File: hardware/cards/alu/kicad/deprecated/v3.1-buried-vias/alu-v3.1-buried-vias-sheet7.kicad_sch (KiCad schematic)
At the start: 8 parts, among them IC1 74*04, IC27 74*86, IC33 74*86, IC34 74*86, IC35 74*283, IC36 74*283, IC37 74*244, IC6 74*08

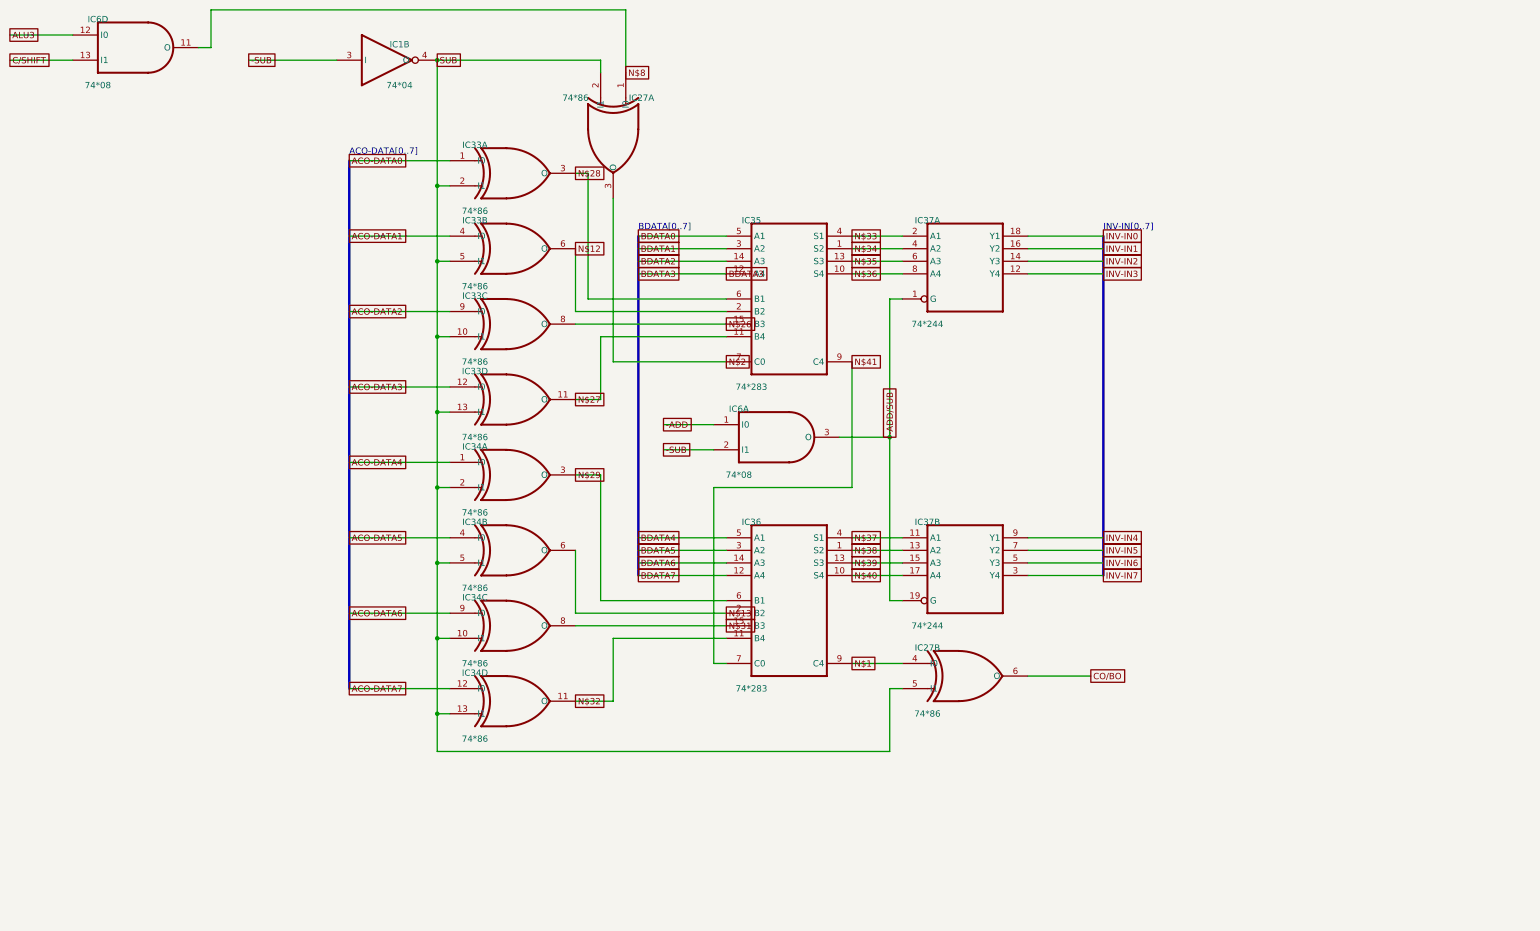
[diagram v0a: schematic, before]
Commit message: fix(kicad): readable converted schematics - overlaps 42,847 -> 3,147, nothing off the frame; CF sheet 0 overlaps
- tools/kicad/sch_overlaps.py: calibrated readability check (text/text, text/body, text/line, off frame/title block)
- eagle_sch_to_kicad.py: fields placed from Eagle's smashed attributes or the symbol's >NAME/>VALUE with Eagle's align,
  size and ratio, readable angles; fields Eagle never shows hidden (FABC96R shows only its pin name); pin numbers hidden
  where every Eagle pin hides them; Eagle-hidden layers dropped (the stray SpiceOrder text); labels on their own wires,
  converter labels only where KiCad needs them; rotate-then-mirror fixed for MR90/MR270 in pin_world/no-connects;
  each sheet on the smallest page that holds it, centred clear of the title block
- finish_board.py: stable footprint-library choice (DRC counts no longer vary run to run)
- all 37 projects regenerated: netlist proofs unchanged (34 MATCH, 2 schematic-only, video Fusion export MISMATCH as
  before); DRC same or better; ERC up (loose wire ends onto graphic buses no longer hidden by labels; explained per README)
- CF card: gate names off the gate bodies, U3 clear of its title, 5.08 mm connector pins; rebuilt: DRC 0/0, proof MATCH
- schematic PDFs regenerated (tools/sch_to_pdf.py, 37/37)

Co-Authored-By: Claude Opus 5.5 <noreply@anthropic.com>
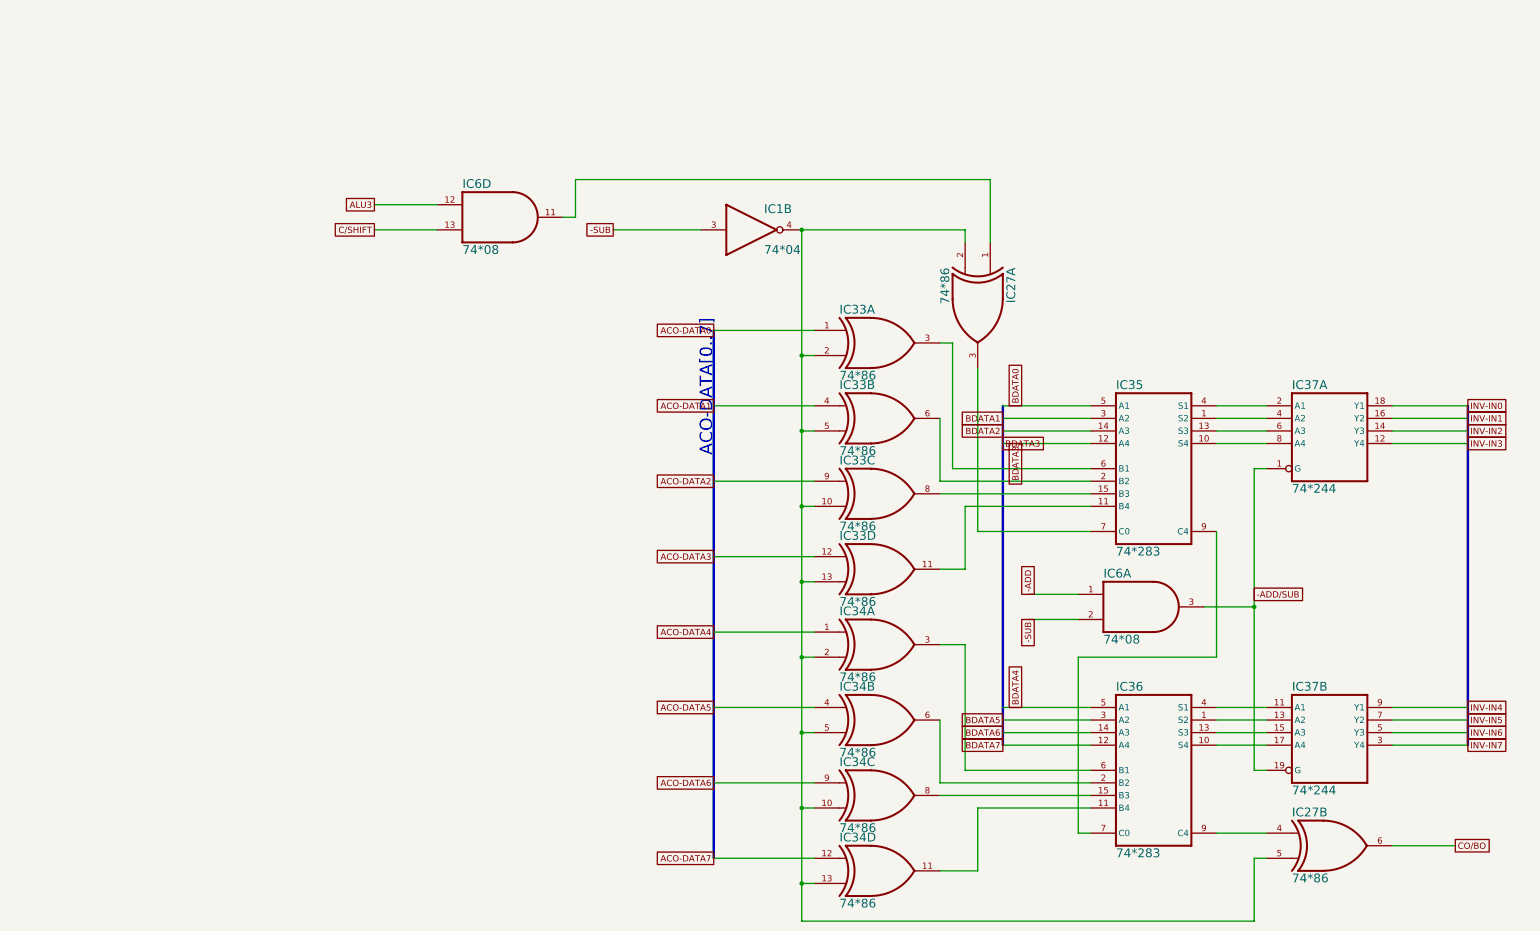
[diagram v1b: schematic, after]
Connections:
- net N$1: no longer names the net of IC27.4 (I0), IC36.9 (C4)
- net N$12: no longer names the net of IC33.6 (O), IC35.2 (B2)
- net N$13: no longer names the net of IC34.6 (O), IC36.2 (B2)
- net N$2: no longer names the net of IC27.3 (O), IC35.7 (C0)
- net N$26: no longer names the net of IC33.8 (O), IC35.15 (B3)
- net N$27: no longer names the net of IC33.11 (O), IC35.11 (B4)
- net N$28: no longer names the net of IC33.3 (O), IC35.6 (B1)
- net N$29: no longer names the net of IC34.3 (O), IC36.6 (B1)
- net N$31: no longer names the net of IC34.8 (O), IC36.15 (B3)
- net N$32: no longer names the net of IC34.11 (O), IC36.11 (B4)
- net N$33: no longer names the net of IC35.4 (S1), IC37.2 (A1)
- net N$34: no longer names the net of IC35.1 (S2), IC37.4 (A2)
- net N$35: no longer names the net of IC35.13 (S3), IC37.6 (A3)
- net N$36: no longer names the net of IC35.10 (S4), IC37.8 (A4)
- net N$37: no longer names the net of IC36.4 (S1), IC37.11 (A1)
- net N$38: no longer names the net of IC36.1 (S2), IC37.13 (A2)
- net N$39: no longer names the net of IC36.13 (S3), IC37.15 (A3)
- net N$40: no longer names the net of IC36.10 (S4), IC37.17 (A4)
- net N$41: no longer names the net of IC35.9 (C4), IC36.7 (C0)
- net N$8: no longer names the net of IC27.1 (I0), IC6.11 (O)
- net SUB: no longer names the net of IC1.4 (O), IC27.2 (I1), IC27.5 (I1), IC33.10 (I1), IC33.13 (I1), IC33.2 (I1), IC33.5 (I1), IC34.10 (I1), IC34.13 (I1), IC34.2 (I1), IC34.5 (I1)
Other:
- note removed: "BDATA[0..7]"
- note removed: "INV-IN[0..7]"
- moved on the sheet: IC35, IC36, IC37A, IC37B
